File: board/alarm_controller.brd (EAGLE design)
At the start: 90 x 65 mm, 149 parts, among them IC3 AT24C, X5 JST-XH-02-PIN-LONG-PAD

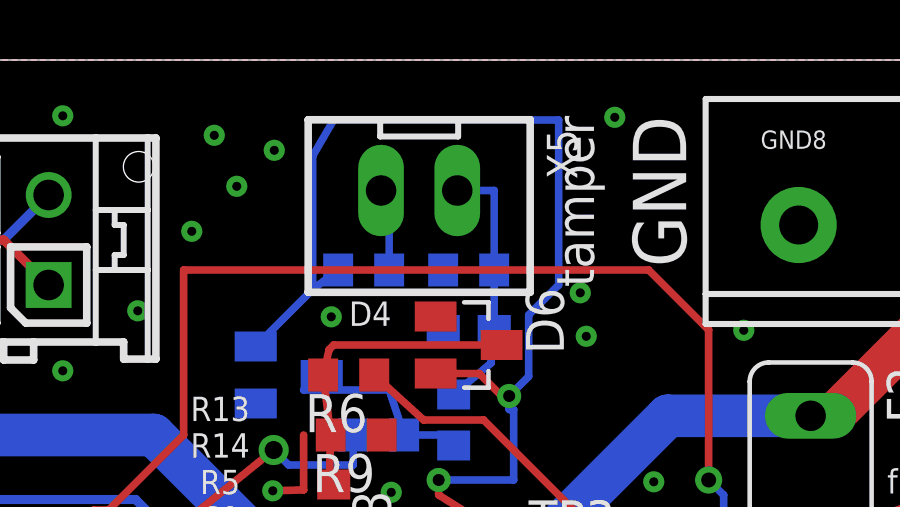
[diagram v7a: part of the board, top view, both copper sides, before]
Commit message: change tamper output to regular 3.5mm screw terminal
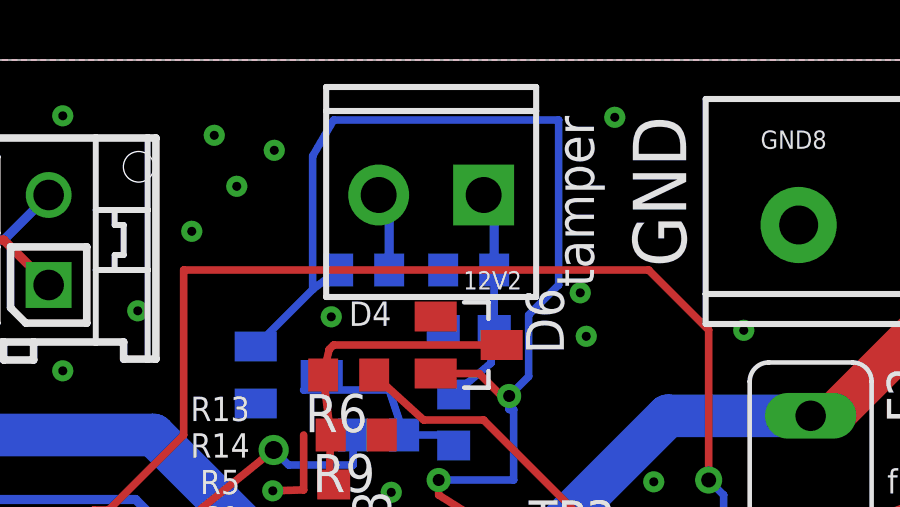
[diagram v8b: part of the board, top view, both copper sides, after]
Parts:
- removed X5: JST-XH-02-PIN-LONG-PAD, Rembrandt Electronics - JST XH Connectors v1-0:JST-XH-02-PACKAGE-LONG-PAD
- added 12V2: (no value), SparkFun-Connectors:SCREWTERMINAL-3.5MM-2
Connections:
- net N$10: now also 12V2.2; no longer X5.2
- net N$11: now also 12V2.1; no longer X5.1
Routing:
- net N$11: track 8.71 -> 7.48 mm
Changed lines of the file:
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@@
 <element name="R2" library="rcl" package="R0603" value="120" x="25.5" y="52" rot="MR180"/>
 <element name="JP2" library="jumper" package="JP1" value="" x="21" y="50.5"/>
-<element name="X5" library="Rembrandt Electronics - JST XH Connectors v1-0" package="JST-XH-02-PACKAGE-LONG-PAD" value="JST-XH-02-PIN-LONG-PAD" x="59.35" y="60.65" rot="R180"/>
+<element name="12V2" library="SparkFun-Connectors" package="SCREWTERMINAL-3.5MM-2" value="" x="61.5" y="60.5" rot="R180">
+<attribute name="PROD_ID" value="CONN-08399" x="61.5" y="60.5" size="1.778" layer="27" rot="R180" display="off"/>
+</element>
 </elements>
 <signals>
@@
 <signal name="N$10">
 <contactref element="R60" pad="1"/>
-<contactref element="X5" pad="2"/>
-<wire x1="58.08" y1="60.65" x2="58.35" y2="60.65" width="0.254" layer="16"/>
-<wire x1="58.35" y1="60.65" x2="58.35" y2="58" width="0.254" layer="16"/>
+<contactref element="12V2" pad="2"/>
+<wire x1="58.35" y1="58" x2="58.35" y2="60.15" width="0.3048" layer="16"/>
+<wire x1="58.35" y1="60.15" x2="58" y2="60.5" width="0.3048" layer="16"/>
 </signal>
 <signal name="TAMPER">
@@
 <wire x1="61.75" y1="54.9" x2="61.75" y2="56" width="0.254" layer="16"/>
 <wire x1="61.75" y1="56" x2="61.85" y2="56" width="0.254" layer="16"/>
-<contactref element="X5" pad="1"/>
-<wire x1="60.62" y1="60.65" x2="61.85" y2="60.65" width="0.254" layer="16"/>
-<wire x1="61.85" y1="60.65" x2="61.85" y2="58" width="0.254" layer="16"/>
+<contactref element="12V2" pad="1"/>
+<wire x1="61.85" y1="58" x2="61.85" y2="60.15" width="0.3048" layer="16"/>
+<wire x1="61.85" y1="60.15" x2="61.5" y2="60.5" width="0.3048" layer="16"/>
 </signal>
 <signal name="PRE_FUSE_12V">
